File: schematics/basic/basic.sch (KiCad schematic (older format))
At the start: 16 parts, among them K1 G5Q-1A, K2 G5Q-1A, Q1 Q_NPN_CBE, Q2 Q_NPN_CBE, SW1 SW_Push, U1 bluepill-STM32F103C8

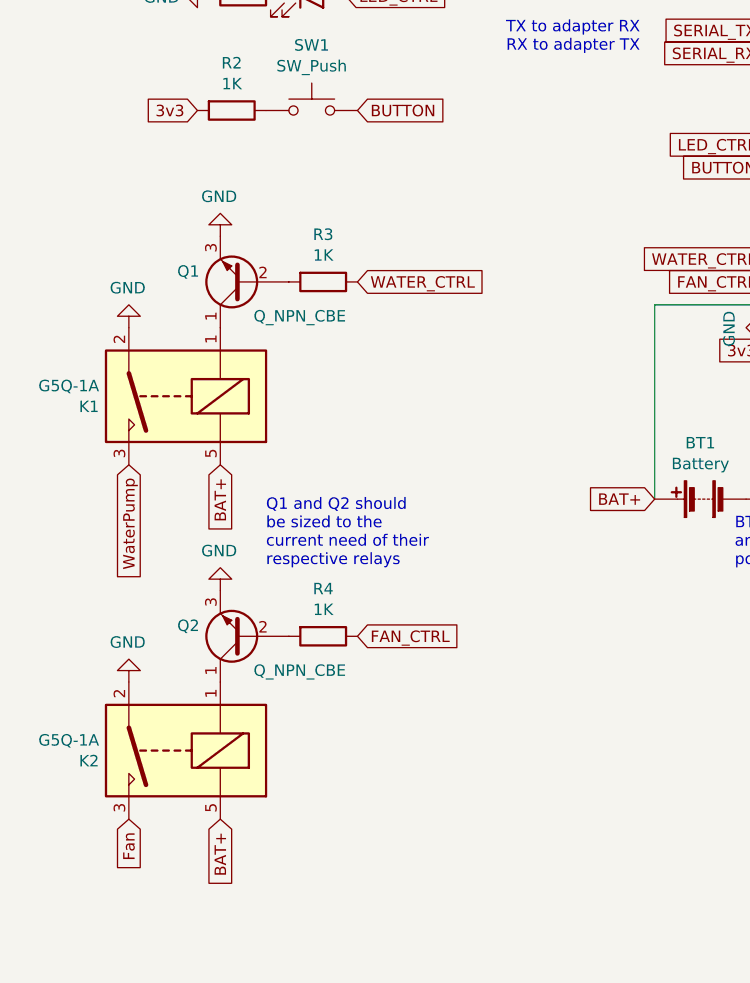
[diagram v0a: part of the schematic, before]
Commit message: Schematics: Add pulldown resistors to NPN bases
How'd I miss those?
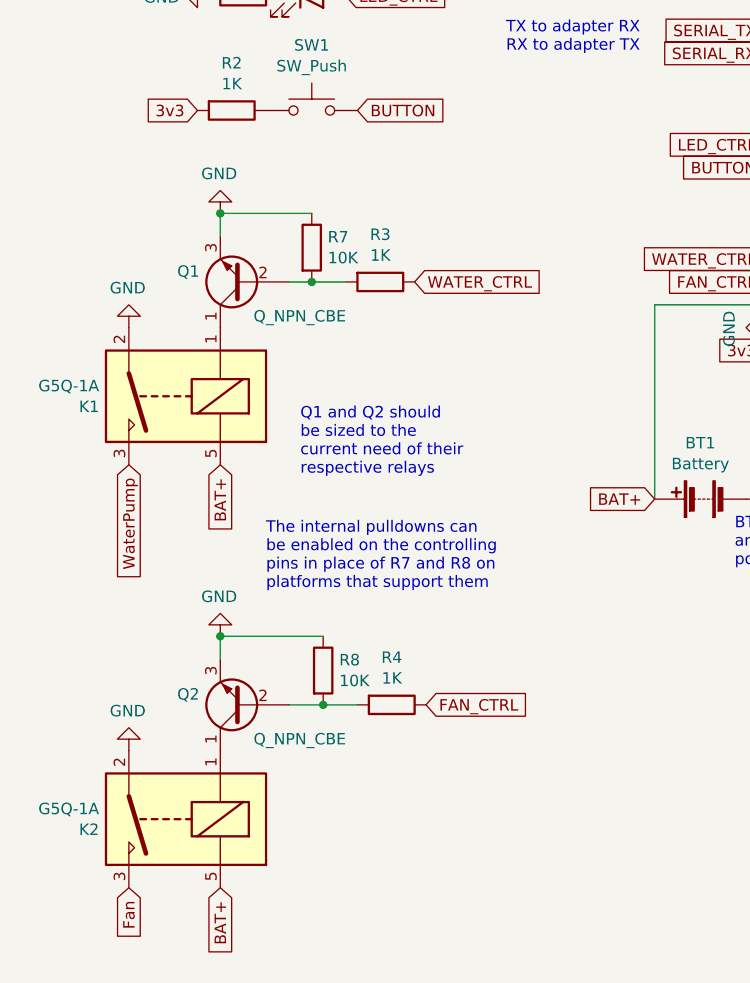
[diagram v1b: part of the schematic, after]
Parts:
- added R7, R8: 10K, symbol Device:R
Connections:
- net GND: now also R7.1, R8.1
- net at Q1.2 (B), R3.2: now also R7.2
- net at Q2.2 (B), R4.2: now also R8.2
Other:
- note added: "The internal pulldowns can\nbe enabled on the controlling\npins in place of R7 and R8 on\nplatforms that support them"
- moved on the sheet: K2, Q2, R3, R4
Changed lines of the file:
@@
 Text GLabel 2050 5200 3    50   Input ~ 0
 WaterPump
+Text GLabel 3300 4400 2    50   Input ~ 0
+WATER_CTRL
+$Comp
+L power:GND #PWR04
+U 1 1 6046ABCD
+P 2450 4100
+F 0 "#PWR04" H 2450 3850 50  0001 C CNN
+F 1 "GND" H 2455 3927 50  0000 C CNN
+F 2 "" H 2450 4100 50  0001 C CNN
+F 3 "" H 2450 4100 50  0001 C CNN
+	1    2450 4100
+	-1   0    0    1
+$EndComp
+Text GLabel 2450 5200 3    50   Input ~ 0
+BAT+
+$Comp
+L Relay:G5Q-1A K2
+U 1 1 6046EE8F
+P 2250 6750
+F 0 "K2" H 2580 6796 50  0000 L CNN
+F 1 "G5Q-1A" H 2580 6705 50  0000 L CNN
+F 2 "Relay_THT:Relay_SPST_Omron-G5Q-1A" H 2600 6700 50  0001 L CNN
+F 3 "https://www.omron.com/ecb/products/pdf/en-g5q.pdf" H 2250 6750 50  0001 C CNN
+	1    2250 6750
+	-1   0    0    1
+$EndComp
+$Comp
+L power:GND #PWR02
+U 1 1 6046EE95
+P 2050 6450
+F 0 "#PWR02" H 2050 6200 50  0001 C CNN
+F 1 "GND" H 2055 6277 50  0000 C CNN
+F 2 "" H 2050 6450 50  0001 C CNN
+F 3 "" H 2050 6450 50  0001 C CNN
+	1    2050 6450
+	-1   0    0    1
+$EndComp
+Text GLabel 2050 7050 3    50   Input ~ 0
+Fan
+$Comp
+L Device:Q_NPN_CBE Q2
+U 1 1 6046EE9C
+P 2550 6250
+F 0 "Q2" H 2741 6204 50  0000 L CNN
+F 1 "Q_NPN_CBE" H 2100 6400 50  0000 L CNN
+F 2 "" H 2750 6350 50  0001 C CNN
+F 3 "~" H 2550 6250 50  0001 C CNN
+	1    2550 6250
+	-1   0    0    1
+$EndComp
+Text GLabel 3350 6250 2    50   Input ~ 0
+FAN_CTRL
+$Comp
+L power:GND #PWR05
+U 1 1 6046EEA3
+P 2450 5950
+F 0 "#PWR05" H 2450 5700 50  0001 C CNN
+F 1 "GND" H 2455 5777 50  0000 C CNN
+F 2 "" H 2450 5950 50  0001 C CNN
+F 3 "" H 2450 5950 50  0001 C CNN
+	1    2450 5950
+	-1   0    0    1
+$EndComp
+Text GLabel 2450 7050 3    50   Input ~ 0
+BAT+
+$Comp
+L Device:R R4
+U 1 1 6047CDB4
+P 3200 6250
+F 0 "R4" V 2993 6250 50  0000 C CNN
+F 1 "1K" V 3084 6250 50  0000 C CNN
+F 2 "" V 3130 6250 50  0001 C CNN
+F 3 "~" H 3200 6250 50  0001 C CNN
+	1    3200 6250
+	0    1    1    0
+$EndComp
+$Comp
+L Device:R R3
+U 1 1 6047D832
+P 3150 4400
+F 0 "R3" V 2943 4400 50  0000 C CNN
+F 1 "1K" V 3034 4400 50  0000 C CNN
+F 2 "" V 3080 4400 50  0001 C CNN
+F 3 "~" H 3150 4400 50  0001 C CNN
+	1    3150 4400
+	0    1    1    0
+$EndComp
+Text GLabel 7400 4750 0    50   Input ~ 0
+SENS_TEMP
+$Comp
+L Device:Thermistor TH1
+U 1 1 60484B2D
+P 7400 4950
+F 0 "TH1" H 7505 4996 50  0000 L CNN
+F 1 "Thermistor" H 7505 4905 50  0000 L CNN
+F 2 "" H 7400 4950 50  0001 C CNN
+F 3 "~" H 7400 4950 50  0001 C CNN
+	1    7400 4950
+	1    0    0    -1
+$EndComp
+$Comp
+L power:GND #PWR09
+U 1 1 60484B33
+P 7400 5150
+F 0 "#PWR09" H 7400 4900 50  0001 C CNN
+F 1 "GND" H 7405 4977 50  0000 C CNN
+F 2 "" H 7400 5150 50  0001 C CNN
+F 3 "" H 7400 5150 50  0001 C CNN
+	1    7400 5150
+	1    0    0    -1
+$EndComp
+Text GLabel 7700 4750 2    50   Input ~ 0
+SENS_PWR
+$Comp
+L Device:R R6
+U 1 1 60484B3A
+P 7550 4750
+F 0 "R6" V 7343 4750 50  0000 C CNN
+F 1 "[Match to TH1]" V 7434 4750 50  0000 C CNN
+F 2 "" V 7480 4750 50  0001 C CNN
+F 3 "~" H 7550 4750 50  0001 C CNN
+	1    7550 4750
+	0    1    1    0
+$EndComp
+$Comp
+L Device:R_Variable HM1
+U 1 1 60487425
+P 7400 3950
+F 0 "HM1" H 7528 3996 50  0000 L CNN
+F 1 "Soil Hygrometer" H 7528 3905 50  0000 L CNN
+F 2 "" V 7330 3950 50  0001 C CNN
+F 3 "~" H 7400 3950 50  0001 C CNN
+	1    7400 3950
+	1    0    0    -1
+$EndComp
+Text GLabel 7400 3800 0    50   Input ~ 0
+SENS_WATER
+$Comp
+L power:GND #PWR08
+U 1 1 60488711
+P 7400 4100
+F 0 "#PWR08" H 7400 3850 50  0001 C CNN
+F 1 "GND" H 7405 3927 50  0000 C CNN
+F 2 "" H 7400 4100 50  0001 C CNN
+F 3 "" H 7400 4100 50  0001 C CNN
+	1    7400 4100
+	1    0    0    -1
+$EndComp
+Text GLabel 7700 3800 2    50   Input ~ 0
+SENS_PWR
+$Comp
+L Device:R R5
+U 1 1 60488718
+P 7550 3800
+F 0 "R5" V 7343 3800 50  0000 C CNN
+F 1 "[Match to HM1]" V 7434 3800 50  0000 C CNN
+F 2 "" V 7480 3800 50  0001 C CNN
+F 3 "~" H 7550 3800 50  0001 C CNN
+	1    7550 3800
+	0    1    1    0
+$EndComp
+Text Notes 4700 5650 0    50   ~ 0
+BT1 should be 4-6V\nand can be any DC\npower source
+$Comp
+L STM32:bluepill-STM32F103C8 U1
+U 1 1 6044A237
+P 5550 3700
+F 0 "U1" H 5450 4865 50  0000 C CNN
+F 1 "bluepill-STM32F103C8" H 5450 4774 50  0000 C CNN
+F 2 "" H 5550 3700 50  0001 C CNN
+F 3 "" H 5550 3700 50  0001 C CNN
+	1    5550 3700
+	1    0    0    -1
+$EndComp
+Wire Wire Line
+	4350 5350 4350 4500
+Wire Wire Line
+	4350 4500 4850 4500
+Text Notes 2800 5250 0    50   ~ 0
+Q1 and Q2 should\nbe sized to the\ncurrent need of their\nrespective relays
 $Comp
 L Device:Q_NPN_CBE Q1
@@
 	-1   0    0    1
 $EndComp
-Text GLabel 3050 4400 2    50   Input ~ 0
-WATER_CTRL
-$Comp
-L power:GND #PWR04
-U 1 1 6046ABCD
-P 2450 4200
-F 0 "#PWR04" H 2450 3950 50  0001 C CNN
-F 1 "GND" H 2455 4027 50  0000 C CNN
-F 2 "" H 2450 4200 50  0001 C CNN
-F 3 "" H 2450 4200 50  0001 C CNN
-	1    2450 4200
-	-1   0    0    1
-$EndComp
-Text GLabel 2450 5200 3    50   Input ~ 0
-BAT+
-$Comp
-L Relay:G5Q-1A K2
-U 1 1 6046EE8F
-P 2250 6450
-F 0 "K2" H 2580 6496 50  0000 L CNN
-F 1 "G5Q-1A" H 2580 6405 50  0000 L CNN
-F 2 "Relay_THT:Relay_SPST_Omron-G5Q-1A" H 2600 6400 50  0001 L CNN
-F 3 "https://www.omron.com/ecb/products/pdf/en-g5q.pdf" H 2250 6450 50  0001 C CNN
-	1    2250 6450
-	-1   0    0    1
-$EndComp
-$Comp
-L power:GND #PWR02
-U 1 1 6046EE95
-P 2050 6150
-F 0 "#PWR02" H 2050 5900 50  0001 C CNN
-F 1 "GND" H 2055 5977 50  0000 C CNN
-F 2 "" H 2050 6150 50  0001 C CNN
-F 3 "" H 2050 6150 50  0001 C CNN
-	1    2050 6150
-	-1   0    0    1
-$EndComp
-Text GLabel 2050 6750 3    50   Input ~ 0
-Fan
-$Comp
-L Device:Q_NPN_CBE Q2
-U 1 1 6046EE9C
-P 2550 5950
-F 0 "Q2" H 2741 5904 50  0000 L CNN
-F 1 "Q_NPN_CBE" H 2100 6100 50  0000 L CNN
-F 2 "" H 2750 6050 50  0001 C CNN
-F 3 "~" H 2550 5950 50  0001 C CNN
-	1    2550 5950
-	-1   0    0    1
-$EndComp
-Text GLabel 3050 5950 2    50   Input ~ 0
-FAN_CTRL
-$Comp
-L power:GND #PWR05
-U 1 1 6046EEA3
-P 2450 5750
-F 0 "#PWR05" H 2450 5500 50  0001 C CNN
-F 1 "GND" H 2455 5577 50  0000 C CNN
-F 2 "" H 2450 5750 50  0001 C CNN
-F 3 "" H 2450 5750 50  0001 C CNN
-	1    2450 5750
-	-1   0    0    1
-$EndComp
-Text GLabel 2450 6750 3    50   Input ~ 0
-BAT+
-$Comp
-L Device:R R4
-U 1 1 6047CDB4
-P 2900 5950
-F 0 "R4" V 2693 5950 50  0000 C CNN
-F 1 "1K" V 2784 5950 50  0000 C CNN
-F 2 "" V 2830 5950 50  0001 C CNN
-F 3 "~" H 2900 5950 50  0001 C CNN
-	1    2900 5950
-	0    1    1    0
-$EndComp
-$Comp
-L Device:R R3
-U 1 1 6047D832
-P 2900 4400
-F 0 "R3" V 2693 4400 50  0000 C CNN
-F 1 "1K" V 2784 4400 50  0000 C CNN
-F 2 "" V 2830 4400 50  0001 C CNN
-F 3 "~" H 2900 4400 50  0001 C CNN
-	1    2900 4400
-	0    1    1    0
-$EndComp
-Text GLabel 7400 4750 0    50   Input ~ 0
-SENS_TEMP
-$Comp
-L Device:Thermistor TH1
-U 1 1 60484B2D
-P 7400 4950
-F 0 "TH1" H 7505 4996 50  0000 L CNN
-F 1 "Thermistor" H 7505 4905 50  0000 L CNN
-F 2 "" H 7400 4950 50  0001 C CNN
-F 3 "~" H 7400 4950 50  0001 C CNN
-	1    7400 4950
-	1    0    0    -1
-$EndComp
-$Comp
-L power:GND #PWR09
-U 1 1 60484B33
-P 7400 5150
-F 0 "#PWR09" H 7400 4900 50  0001 C CNN
-F 1 "GND" H 7405 4977 50  0000 C CNN
-F 2 "" H 7400 5150 50  0001 C CNN
-F 3 "" H 7400 5150 50  0001 C CNN
-	1    7400 5150
-	1    0    0    -1
-$EndComp
-Text GLabel 7700 4750 2    50   Input ~ 0
-SENS_PWR
-$Comp
-L Device:R R6
-U 1 1 60484B3A
-P 7550 4750
-F 0 "R6" V 7343 4750 50  0000 C CNN
-F 1 "[Match to TH1]" V 7434 4750 50  0000 C CNN
-F 2 "" V 7480 4750 50  0001 C CNN
-F 3 "~" H 7550 4750 50  0001 C CNN
-	1    7550 4750
-	0    1    1    0
-$EndComp
-$Comp
-L Device:R_Variable HM1
-U 1 1 60487425
-P 7400 3950
-F 0 "HM1" H 7528 3996 50  0000 L CNN
-F 1 "Soil Hygrometer" H 7528 3905 50  0000 L CNN
-F 2 "" V 7330 3950 50  0001 C CNN
-F 3 "~" H 7400 3950 50  0001 C CNN
-	1    7400 3950
-	1    0    0    -1
-$EndComp
-Text GLabel 7400 3800 0    50   Input ~ 0
-SENS_WATER
-$Comp
-L power:GND #PWR08
-U 1 1 60488711
-P 7400 4100
-F 0 "#PWR08" H 7400 3850 50  0001 C CNN
-F 1 "GND" H 7405 3927 50  0000 C CNN
-F 2 "" H 7400 4100 50  0001 C CNN
-F 3 "" H 7400 4100 50  0001 C CNN
-	1    7400 4100
-	1    0    0    -1
-$EndComp
-Text GLabel 7700 3800 2    50   Input ~ 0
-SENS_PWR
-$Comp
-L Device:R R5
-U 1 1 60488718
-P 7550 3800
-F 0 "R5" V 7343 3800 50  0000 C CNN
-F 1 "[Match to HM1]" V 7434 3800 50  0000 C CNN
-F 2 "" V 7480 3800 50  0001 C CNN
-F 3 "~" H 7550 3800 50  0001 C CNN
-	1    7550 3800
-	0    1    1    0
-$EndComp
-Text Notes 4700 5650 0    50   ~ 0
-BT1 should be 4-6V\nand can be any DC\npower source
-$Comp
-L STM32:bluepill-STM32F103C8 U1
-U 1 1 6044A237
-P 5550 3700
-F 0 "U1" H 5450 4865 50  0000 C CNN
-F 1 "bluepill-STM32F103C8" H 5450 4774 50  0000 C CNN
-F 2 "" H 5550 3700 50  0001 C CNN
-F 3 "" H 5550 3700 50  0001 C CNN
-	1    5550 3700
-	1    0    0    -1
-$EndComp
-Wire Wire Line
-	4350 5350 4350 4500
-Wire Wire Line
-	4350 4500 4850 4500
-Text Notes 2650 5650 0    50   ~ 0
-Q1 and Q2 should\nbe sized to the\ncurrent need of their\nrespective relays
+$Comp
+L Device:R R7
+U 1 1 6090929A
+P 2850 4250
+F 0 "R7" H 2920 4296 50  0000 L CNN
+F 1 "10K" H 2920 4205 50  0000 L CNN
+F 2 "" V 2780 4250 50  0001 C CNN
+F 3 "~" H 2850 4250 50  0001 C CNN
+	1    2850 4250
+	1    0    0    -1
+$EndComp
+Wire Wire Line
+	2850 4100 2450 4100
+Wire Wire Line
+	2450 4100 2450 4200
+Connection ~ 2450 4100
+Wire Wire Line
+	3000 4400 2850 4400
+Wire Wire Line
+	2750 4400 2850 4400
+Connection ~ 2850 4400
+$Comp
+L Device:R R8
+U 1 1 6090B1B6
+P 2900 6100
+F 0 "R8" H 2970 6146 50  0000 L CNN
+F 1 "10K" H 2970 6055 50  0000 L CNN
+F 2 "" V 2830 6100 50  0001 C CNN
+F 3 "~" H 2900 6100 50  0001 C CNN
+	1    2900 6100
+	1    0    0    -1
+$EndComp
+Wire Wire Line
+	2900 5950 2450 5950
+Wire Wire Line
+	2450 5950 2450 6050
+Connection ~ 2450 5950
+Wire Wire Line
+	2900 6250 2750 6250
+Wire Wire Line
+	2900 6250 3050 6250
+Connection ~ 2900 6250
+Text Notes 2650 5750 0    50   ~ 0
+The internal pulldowns can\nbe enabled on the controlling\npins in place of R7 and R8 on\nplatforms that support them
 $EndSCHEMATC
